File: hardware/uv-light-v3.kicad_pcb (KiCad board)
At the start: 2 copper layers, 25 x 15 mm, 25 parts, among them P1 CON-SENSOR2, P2 DEBUG, P3 BOOT, U1 XMC1100, U2 AS7331, U3 DRILL, U4 DRILL, U5 DRILL, U6 DRILL

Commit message: first pcb layout
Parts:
- added VAL: CE_5mm, kicad-libraries:CE_5mm, B.Cu at (135.8, 84.1)
- G***: moved to B.Cu
- moved G*** 22.4 mm to (126.3, 86.4), turned to -90 degrees
- moved VAL 11.4 mm to (142.8, 87.8), turned to -90 degrees
- moved C6 8.58 mm to (143.4, 85.4), turned to 180 degrees
- moved C5 8.50 mm to (143.4, 90.6), turned to 180 degrees
- moved R2 6.38 mm to (145.6, 87.9), turned to 90 degrees
- moved G*** 3.14 mm to (135.7, 90.8), turned to -90 degrees
- moved P2 1.17 mm to (137.1, 93.3)
- moved U2 0.10 mm to (143.4, 88.0)
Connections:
- RP2 pad 5: SCL -> SDA
- RP2 pad 8: SDA -> SCL
- U1 pad 13: unconnected-(U1-Pad13) -> SYN
- U1 pad 14: unconnected-(U1-Pad14) -> READY
- U1 pad 20: SYN -> unconnected-(U1-Pad20)
- U1 pad 21: READY -> unconnected-(U1-Pad21)
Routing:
- net SYN: track 0.00 -> 15.4 mm, vias 0 -> 2
- net VCC: track 56.7 -> 71.8 mm
- net READY: track 0.00 -> 13.3 mm, vias 0 -> 2
- net GND: track 21.5 -> 32.7 mm, vias 9 -> 13
- net SDA: track 6.35 -> 9.61 mm, vias 2 -> 0
- net Net-(R2-Pad2): track 0.00 -> 1.75 mm
- net Net-(P2-Pad1): track 1.28 -> 2.25 mm
- net SCL: track 8.34 -> 8.23 mm, vias 2 -> 0
- added copper zone on F.Cu, net GND

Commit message: ready for prototype
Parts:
- RP2: value 2k2 -> 1k
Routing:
- net GND: track 32.7 -> 43.9 mm
- removed copper zone on F.Cu, net GND
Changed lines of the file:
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@@
       (effects (font (size 0.29972 0.29972) (thickness 0.07493)))
     )
-    (fp_text value "2k2" (at 1.00076 0) (layer "F.Fab")
+    (fp_text value "1k" (at 1.00076 0) (layer "F.Fab")
       (effects (font (size 0.29972 0.29972) (thickness 0.07493)))
     )
@@
   (segment (start 142.35 85.7) (end 142.65 85.4) (width 0.25) (layer "F.Cu") (net 1))
   (segment (start 140.32 88.5) (end 139.85 88.5) (width 0.55) (layer "F.Cu") (net 1))
+  (segment (start 145.55 88.65) (end 144.65 87.75) (width 0.25) (layer "F.Cu") (net 1))
+  (segment (start 143.15 86.95) (end 143.15 86.425) (width 0.25) (layer "F.Cu") (net 1))
   (segment (start 142.65 90.95) (end 142.3 91.3) (width 0.25) (layer "F.Cu") (net 1))
   (segment (start 142.65 90.6) (end 142.65 90.95) (width 0.25) (layer "F.Cu") (net 1))
@@
   (segment (start 133.8 92.119239) (end 132.880761 91.2) (width 0.3) (layer "F.Cu") (net 1))
   (segment (start 142.65 86.425) (end 143.15 86.425) (width 0.25) (layer "F.Cu") (net 1))
-  (segment (start 145.2 88.65) (end 144.8 88.25) (width 0.25) (layer "F.Cu") (net 1))
+  (segment (start 142.35 87.25) (end 142.65 86.95) (width 0.25) (layer "F.Cu") (net 1))
+  (segment (start 144.45 87.75) (end 144.45 87.25) (width 0.25) (layer "F.Cu") (net 1))
+  (segment (start 144.65 87.75) (end 144.45 87.75) (width 0.25) (layer "F.Cu") (net 1))
   (segment (start 133.8 90.280761) (end 134.719239 91.2) (width 0.3) (layer "F.Cu") (net 1))
   (segment (start 142.65 85.4) (end 142.2 85.4) (width 0.25) (layer "F.Cu") (net 1))
@@
   (segment (start 143.15 89.575) (end 143.15 90.1) (width 0.25) (layer "F.Cu") (net 1))
   (segment (start 142.65 91.05) (end 142.9 91.3) (width 0.25) (layer "F.Cu") (net 1))
+  (segment (start 142.35 87.25) (end 142.35 87.75) (width 0.25) (layer "F.Cu") (net 1))
+  (segment (start 142.65 86.95) (end 142.65 86.425) (width 0.25) (layer "F.Cu") (net 1))
   (segment (start 143.15 85.9) (end 143.15 86.425) (width 0.25) (layer "F.Cu") (net 1))
   (segment (start 143.15 90.1) (end 142.65 90.6) (width 0.25) (layer "F.Cu") (net 1))
   (segment (start 140.30076 87) (end 140.30076 87.57924) (width 0.55) (layer "F.Cu") (net 1))
   (segment (start 142.65 85.4) (end 143.15 85.9) (width 0.25) (layer "F.Cu") (net 1))
+  (segment (start 142.35 88.25) (end 140.64 88.25) (width 0.25) (layer "F.Cu") (net 1))
+  (segment (start 144.45 88.25) (end 142.35 88.25) (width 0.25) (layer "F.Cu") (net 1))
   (segment (start 142.2 85.4) (end 141.9 85.1) (width 0.25) (layer "F.Cu") (net 1))
+  (segment (start 143.45 87.25) (end 143.15 86.95) (width 0.25) (layer "F.Cu") (net 1))
   (segment (start 132.191332 92.455115) (end 132.204885 92.455115) (width 0.2) (layer "F.Cu") (net 1))
   (segment (start 142.2 85.4) (end 141.9 85.7) (width 0.25) (layer "F.Cu") (net 1))
-  (segment (start 144.8 88.25) (end 144.45 88.25) (width 0.25) (layer "F.Cu") (net 1))
+  (segment (start 140.64 88.25) (end 140.58 88.19) (width 0.25) (layer "F.Cu") (net 1))
+  (segment (start 143.45 87.25) (end 142.35 87.25) (width 0.25) (layer "F.Cu") (net 1))
+  (segment (start 145.6 88.65) (end 145.55 88.65) (width 0.25) (layer "F.Cu") (net 1))
   (segment (start 141.9 85.1) (end 142.35 85.1) (width 0.25) (layer "F.Cu") (net 1))
-  (segment (start 145.6 88.65) (end 145.2 88.65) (width 0.25) (layer "F.Cu") (net 1))
+  (segment (start 142.35 87.75) (end 144.45 87.75) (width 0.25) (layer "F.Cu") (net 1))
+  (segment (start 144.45 87.25) (end 143.45 87.25) (width 0.25) (layer "F.Cu") (net 1))
   (via (at 130.8 84.8) (size 0.55) (drill 0.25) (layers "F.Cu" "B.Cu") (net 1))
   (via (at 132.1 86.2) (size 0.55) (drill 0.25) (layers "F.Cu" "B.Cu") (net 1))
@@
   (segment (start 141.15 93.9) (end 144.979685 90.070315) (width 0.2) (layer "B.Cu") (net 33))
   (segment (start 144.979685 90.070315) (end 144.979685 89.960157) (width 0.2) (layer "B.Cu") (net 33))
-  (zone (net 1) (net_name "GND") (layer "F.Cu") (hatch edge 0.508)
-    (connect_pads yes (clearance 0.15))
-    (min_thickness 0.254) (filled_areas_thickness no)
-    (fill yes (thermal_gap 0.508) (thermal_bridge_width 0.508))
-    (polygon
-      (pts
-        (xy 143.3 85.8)
-        (xy 143.3 87)
-        (xy 144.6 87)
-        (xy 144.6 88.4)
-        (xy 142.2 88.4)
-        (xy 142.2 85.6)
-        (xy 142.5 85.6)
-        (xy 142.5 85.6)
-        (xy 143.1 85.6)
-      )
-    )
-  )
   (zone (net 1) (net_name "GND") (layer "B.Cu") (hatch edge 0.508)
     (connect_pads yes (clearance 0.15))

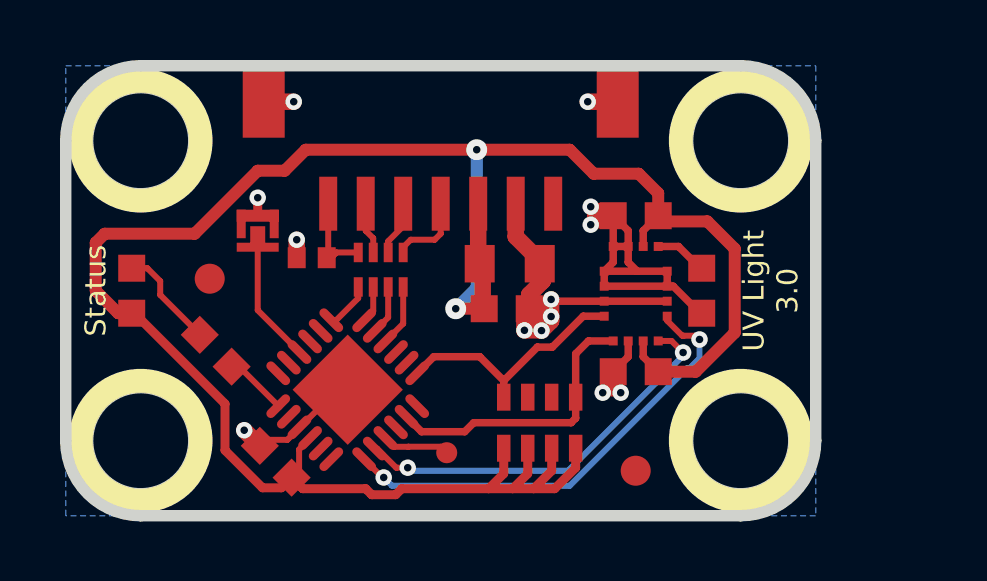
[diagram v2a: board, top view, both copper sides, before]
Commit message: changed mask layer to 0mm cutout, removed traces under AS7331
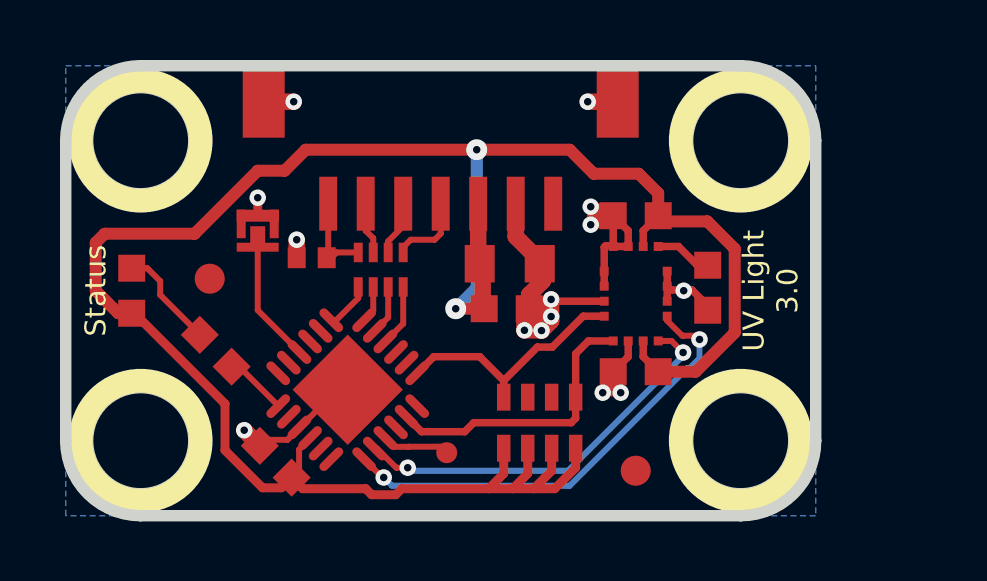
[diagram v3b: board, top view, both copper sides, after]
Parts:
- moved R2 0.22 mm to (145.8, 87.8)
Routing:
- net GND: track 43.9 -> 37.6 mm, vias 13 -> 14
